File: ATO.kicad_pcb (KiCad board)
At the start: 2 copper layers, 42.2 x 43.2 mm, 20 parts, among them J1 Pump Out, J2 Switch, J3 Power, Q1 Q_NMOS_GDSD, Q2 PFET, Q3 NFET, Q4 PFET, SW1 Reset, SW2 Fill

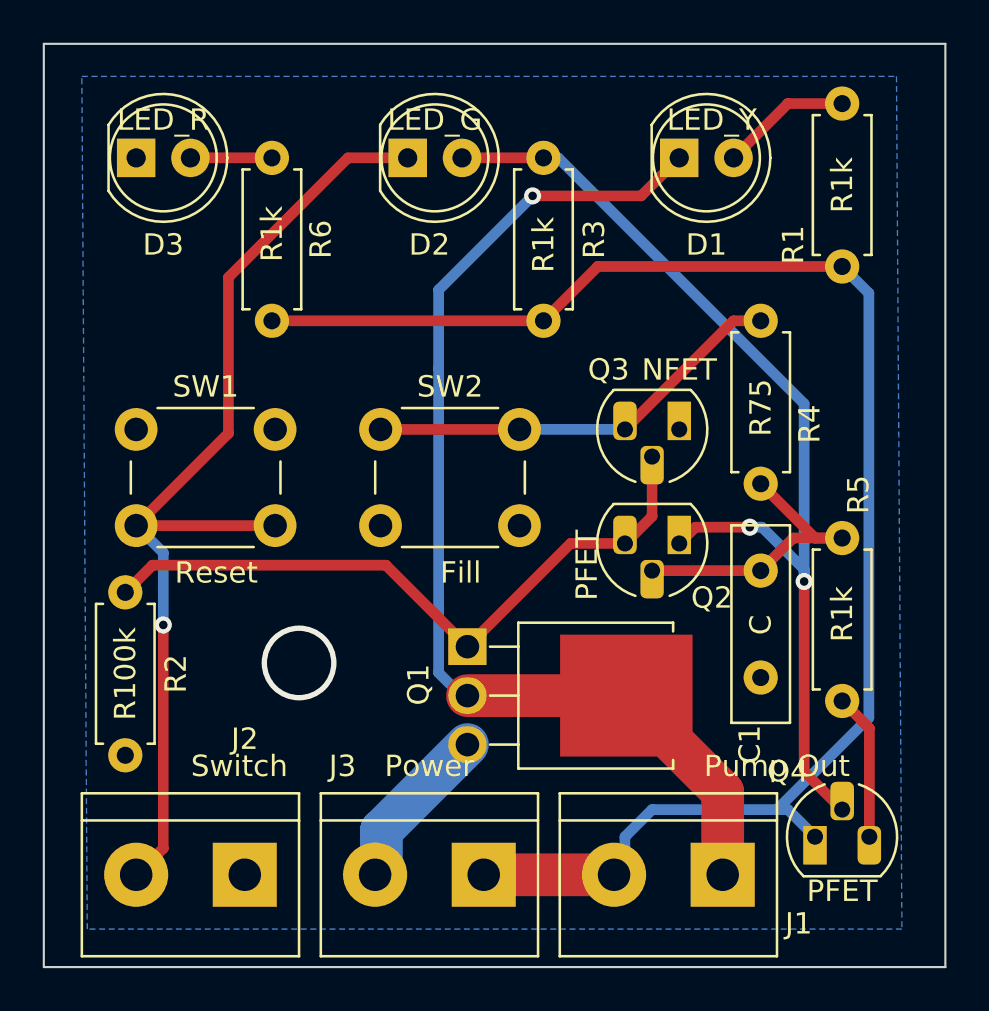
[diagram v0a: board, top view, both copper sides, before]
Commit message: Added cap on power input and other tweaks.
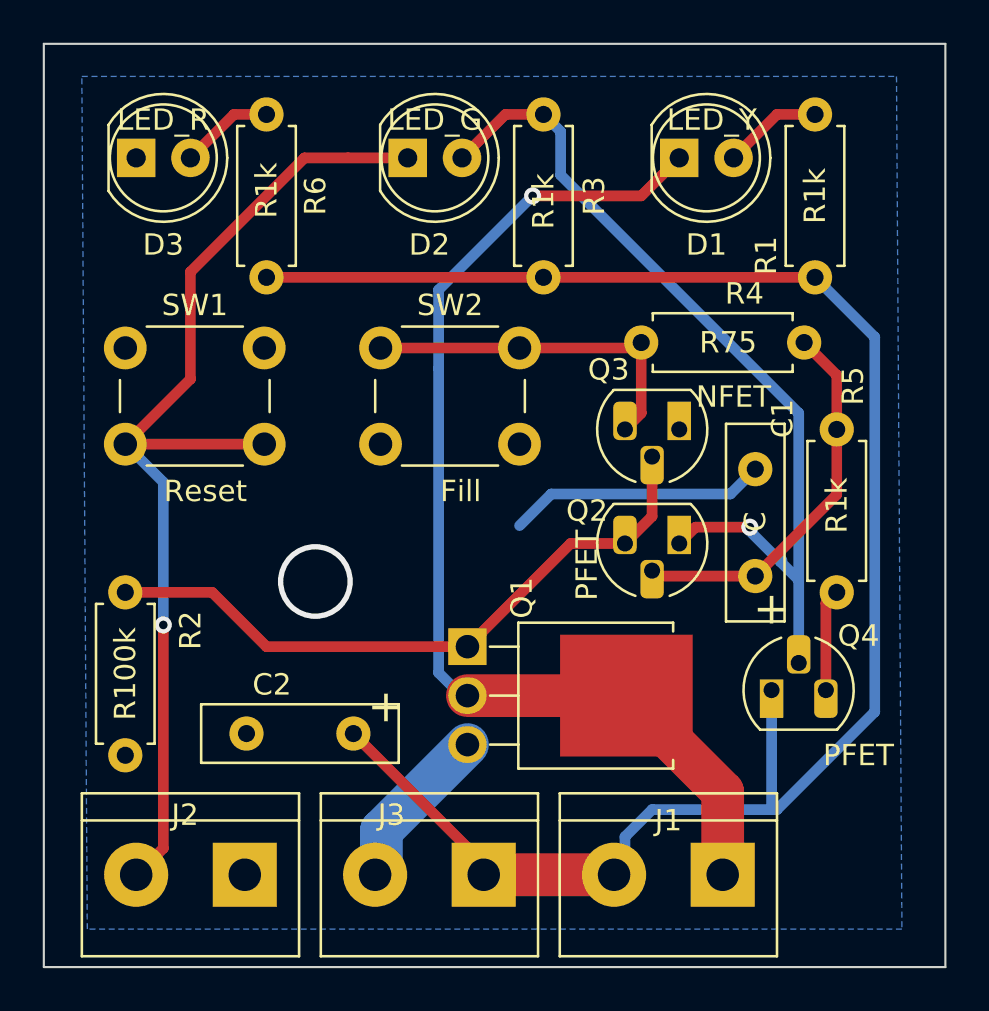
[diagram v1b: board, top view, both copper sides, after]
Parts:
- added C2: CP, Capacitor_THT:C_Disc_D9.0mm_W2.5mm_P5.00mm, F.Cu at (69.8, 103.1)
- Q1: value Q_NMOS_GDSD -> NFET
- moved Q4 7.15 mm to (89.4, 101.1)
- moved R4 6.91 mm to (90.9, 84.8), turned to 180 degrees
- moved R5 5.09 mm to (92.5, 96.5)
- moved SW1 3.84 mm to (59.2, 85.1)
- moved SW2 3.81 mm to (71.1, 85.1)
- moved R6 2.05 mm to (65.8, 81.8)
- moved R3 2.03 mm to (78.7, 74.2)
- moved R1 1.37 mm to (91.4, 81.8)
- moved C1 0.36 mm to (88.6, 95.8), turned to 90 degrees
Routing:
- net GND: track 7.25 -> 19.4 mm
- net Net-(C2-Pad1): track 72.7 -> 83.3 mm
- net Net-(D2-Pad2): track 48.0 -> 42.4 mm, vias 2 -> 1
- net Net-(C1-Pad1): track 14.4 -> 18.1 mm
- net Net-(Q3-Pad3): track 19.9 -> 16.7 mm
- net Net-(Q4-Pad3): track 6.88 -> 5.04 mm
- net Net-(D1-Pad2): track 6.13 -> 4.65 mm
- net Net-(Q1-Pad1): track 32.1 -> 31.0 mm
- net Net-(D2-Pad1): track 48.0 -> 48.9 mm
- net Net-(D3-Pad2): track 3.81 -> 4.40 mm
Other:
- board text added: "+"
- board text added: "OSH-ATO Input Voltage: 5V-18V Float switch must be closed when water level high Max pump current: 2A (1oz) / 4A (2oz) github.com/whendonkiesfly/OSHOTA"
- board text removed: "OSH-ATO Input Voltage: 5V-18V Float switch must be closed when water level high github.com/whendonkiesfly/OSHOTA"
